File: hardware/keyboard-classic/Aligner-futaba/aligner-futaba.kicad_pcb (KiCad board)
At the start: 2 copper layers, 307.3 x 103.9 mm, 72 parts, among them SW1 Clear, SW10 Bracket_Open, SW11 6, SW12 Y, SW13 Return, SW14 Dash, SW15 5, SW16 T, SW17 Line Feed, SW18 Colon, SW19 4, SW2 Repeat, SW20 R, SW21 O, SW22 0, SW23 3, SW24 E, SW25 L, SW26 9, SW27 2, SW28 W, SW29 Period, SW3 Tilde, SW30 8, SW31 1, SW32 Ampersand, SW33 Break, SW34 Rubout, SW35 R_Shift, SW36 P, SW37 Comma, SW38 K, SW39 L_Shift, SW4 I, SW40 Semicolon, SW41 M, SW42 J, SW43 Fwd_Slash, SW44 N, SW45 H, SW46 SPACE, SW47 B, SW48 G, SW49 ESC, SW5 Here_is, SW50 Z, SW51 V, SW52 F, SW53 CTRL, SW54 A, SW55 C, SW56 D, SW57 Backslash, SW58 Q, SW59 X, SW6 Bracket_Close, SW60 S, SW7 7, SW8 U, SW9 Shift_Lock

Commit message: OSI mounting holes
- Add OSI-compatible mounting holes.
- Adjust keyboard and aligner holes to make room for the OSI mounting holes
- Change "Universal Keyboard" to "Unified Keyboard" in the design files.
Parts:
- removed the REF** at (107.8, 171.4)
- removed the REF** at (284.6, 171.4)
- removed the REF** at (363.2, 171.4)
- added REF**: MountingHole_3.5mm, MountingHole:MountingHole_3.5mm, F.Cu at (102.7, 171.4)
- added REF**: MountingHole_3.5mm, MountingHole:MountingHole_3.5mm, F.Cu at (289.7, 171.4)
- added REF**: MountingHole_3.5mm, MountingHole:MountingHole_3.5mm, F.Cu at (358.1, 171.4)
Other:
- board text added: "Unified Keyboard Rev 1.2 http://osiweb.org Key Aligner for Futaba MD-4PCS, George Risk KBM-01-01"
- board text removed: "Universal Keyboard Rev 1.1 http://osiweb.org Key Aligner for Futaba MD-4PCS, George Risk KBM-01-01"

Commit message: Finalize layout and mounting
- Add apple 2 mounting slots (and stretch PCB to accommodate slots
- Add pass-through holes in aligners for OSI keyboard spacers
- Move 'ESC' key next to '1' key
- Add TAB key next to Q key
- remove 'here is' and finalize "helper" keys along left side of keyboard
- move legends off of PCB traces
- update to release 1.3
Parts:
- removed the REF** at (72.1, 148.3)
- added REF**: FN, unikbd:Futaba-MD-4PCS-aligner, F.Cu at (82.8, 166.1)
- added REF**: OSI mounting holes, unikbd:OSI_spacer_holes, F.Cu at (196.9, 166.0)
- added REF**: OSHW-Logo2_9.8x8mm_SilkScreen, Symbol:OSHW-Logo2_9.8x8mm_SilkScreen, F.Cu at (146.6, 174.7)
- added SW62: ESC, unikbd:Futaba-MD-4PCS-aligner, F.Cu at (68.6, 89.8)
- SW1: value Clear -> RT arrow
- SW2: value Repeat -> LT arrow
- SW32: value Ampersand -> @ (at symbol)
- SW49: value ESC -> Tab
- SW5: value Here_is -> Repeat
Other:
- board size 307.3 x 103.9 mm -> 312.4 x 114 mm
- board text added: "Unified Keyboard Rev 1.3 http://osiweb.org Key Aligner for Futaba MD-4PCS, George Risk KBM-01-01"
- board text removed: "Unified Keyboard Rev 1.2 http://osiweb.org Key Aligner for Futaba MD-4PCS, George Risk KBM-01-01"

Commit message: Keyboard layout updates
- Add extra key to the left side of row 4 to permit "inverted T" for those who
  want it.

- Tiny shifts of several keys to correct key distances

- Include mounting holes with daughter board connector, to ensure consistency.
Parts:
- added REF**: Cherry aligner, unikbd:Cherry aligner, F.Cu at (263.8, 166.0)
- added REF**: Cherry aligner, unikbd:Cherry aligner, F.Cu at (130.5, 166.0)
- moved SW12 0.28 mm to (192.4, 108.8)
- moved SW17 0.28 mm to (287.6, 108.8)
- moved SW20 0.28 mm to (154.3, 108.8)
- moved SW22 0.28 mm to (249.5, 108.8)
- moved SW36 0.28 mm to (268.6, 108.8)
- moved SW8 0.28 mm to (211.4, 108.8)
- moved SW28 0.28 mm to (116.2, 108.8)
- moved SW58 0.28 mm to (97.1, 108.8)
- moved SW16 0.28 mm to (173.3, 108.8)
- moved SW24 0.28 mm to (135.2, 108.8)
- moved SW4 0.28 mm to (230.5, 108.8)
- moved SW13 0.24 mm to (311.5, 108.8)
- moved REF** 0.22 mm to (197.2, 166.0)
- moved SW46 0.22 mm to (197.2, 166.0)
- moved SW33 0.20 mm to (354.3, 108.8)
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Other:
- outline, holes or cut-outs redrawn
- board text added: "Unified Keyboard Rev 1.4 http://osiweb.org Key Aligner for Futaba MD-4PCS, George Risk KBM-01-01"
- board text removed: "Unified Keyboard Rev 1.3 http://osiweb.org Key Aligner for Futaba MD-4PCS, George Risk KBM-01-01"

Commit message: Moved mounting slots from keyboard PCB to aligners
- This allows the PCB to sink below the mounting brackets.  The aligner height can
be adjusted relative to the mounting brackets using spacers.

- changed futaba aligners to use cherry stabilizers.

- bumped rev number
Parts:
- removed the REF** at (263.8, 166.0)
- removed the REF** at (130.5, 166.0)
- SW46: footprint unikbd:Futaba-MD-4PCS-aligner -> unikbd:Futaba_space_Cherry_aligner
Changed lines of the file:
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@@
     (tracks 0)
     (zones 0)
-    (modules 77)
+    (modules 75)
     (nets 1)
   )
@@
     (visible_elements 7FFFEFFF)
     (pcbplotparams
-      (layerselection 0x010fc_ffffffff)
+      (layerselection 0x010f0_ffffffff)
       (usegerberextensions false)
       (usegerberattributes false)
@@
       (drillshape 0)
       (scaleselection 1)
-      (outputdirectory "futaba-aligner-outputs"))
+      (outputdirectory "outputs"))
   )
   (net 0 "")
@@
     (diff_pair_gap 0.254)
   )
-  (module "unikbd:Cherry aligner" (layer F.Cu)
-    (at 263.83488 165.99916)
-    (fp_text reference REF** (at -5.0292 -7.7724) (layer F.SilkS)
-      (effects (font (size 1 1) (thickness 0.15)))
-    )
-    (fp_text value "Cherry aligner" (at 0 7.9756) (layer B.Fab)
-      (effects (font (size 1 1) (thickness 0.15)))
-    )
-    (fp_line (start -6.985 -6.985) (end -6.985 6.985) (layer Edge.Cuts) (width 0.12))
-    (fp_line (start 6.985 6.985) (end 6.985 -6.985) (layer Edge.Cuts) (width 0.12))
-    (fp_line (start -6.985 -6.985) (end 6.985 -6.985) (layer Edge.Cuts) (width 0.12))
-    (fp_line (start -6.985 6.985) (end 6.985 6.985) (layer Edge.Cuts) (width 0.12))
-  )
-  (module "unikbd:Cherry aligner" (layer F.Cu)
-    (at 130.48488 165.99916)
-    (fp_text reference REF** (at -5.0292 -7.7724) (layer F.SilkS)
-      (effects (font (size 1 1) (thickness 0.15)))
-    )
-    (fp_text value "Cherry aligner" (at 0 7.9756) (layer B.Fab)
-      (effects (font (size 1 1) (thickness 0.15)))
-    )
-    (fp_line (start -6.985 -6.985) (end -6.985 6.985) (layer Edge.Cuts) (width 0.12))
-    (fp_line (start 6.985 6.985) (end 6.985 -6.985) (layer Edge.Cuts) (width 0.12))
-    (fp_line (start -6.985 -6.985) (end 6.985 -6.985) (layer Edge.Cuts) (width 0.12))
-    (fp_line (start -6.985 6.985) (end 6.985 6.985) (layer Edge.Cuts) (width 0.12))
+  (module unikbd:Futaba_space_Cherry_aligner (layer F.Cu)
+    (at 197.15988 165.99916)
+    (fp_text reference SW46 (at -4.62788 -8.77316) (layer F.SilkS)
+      (effects (font (size 1 1) (thickness 0.15)))
+    )
+    (fp_text value SPACE (at -3.35788 9.00684) (layer F.SilkS)
+      (effects (font (size 1 1) (thickness 0.15)))
+    )
+    (fp_text user MX_space_aligner (at -0.6096 7.9248) (layer B.Fab)
+      (effects (font (size 1 1) (thickness 0.15)))
+    )
+    (fp_text user SW** (at -5.334 -7.874) (layer F.SilkS)
+      (effects (font (size 1 1) (thickness 0.15)))
+    )
+    (fp_text user Futaba_2u_Cherry_aligner (at 0 -0.5) (layer F.Fab)
+      (effects (font (size 1 1) (thickness 0.15)))
+    )
+    (fp_text user REF** (at 0 0.5) (layer F.SilkS) hide
+      (effects (font (size 1 1) (thickness 0.15)))
+    )
+    (fp_line (start -63.3476 1.397) (end -7.6962 1.397) (layer Edge.Cuts) (width 0.12))
+    (fp_line (start -63.3476 -1.397) (end -7.6962 -1.397) (layer Edge.Cuts) (width 0.12))
+    (fp_line (start 7.6962 -1.397) (end 63.3476 -1.397) (layer Edge.Cuts) (width 0.12))
+    (fp_line (start 7.6962 1.397) (end 63.3476 1.397) (layer Edge.Cuts) (width 0.12))
+    (fp_arc (start 0 0) (end 7.697216 -1.397) (angle -159.4) (layer Edge.Cuts) (width 0.12))
+    (fp_arc (start 0 0) (end -7.697216 1.397) (angle -159.4) (layer Edge.Cuts) (width 0.12))
+    (fp_line (start 63.3476 -1.397) (end 63.3476 -5.6896) (layer Edge.Cuts) (width 0.12))
+    (fp_line (start 63.3476 -5.6896) (end 70.0024 -5.6896) (layer Edge.Cuts) (width 0.12))
+    (fp_line (start 70.0024 -5.6896) (end 70.0024 -2.286) (layer Edge.Cuts) (width 0.12))
+    (fp_line (start 70.0024 -2.286) (end 70.866 -2.286) (layer Edge.Cuts) (width 0.12))
+    (fp_line (start 70.866 -2.286) (end 70.866 0.508) (layer Edge.Cuts) (width 0.12))
+    (fp_line (start 70.866 0.508) (end 70.0024 0.508) (layer Edge.Cuts) (width 0.12))
+    (fp_line (start 70.0024 0.508) (end 70.0024 6.604) (layer Edge.Cuts) (width 0.12))
+    (fp_line (start 70.0024 6.604) (end 68.199 6.604) (layer Edge.Cuts) (width 0.12))
+    (fp_line (start 68.199 6.604) (end 68.199 7.7724) (layer Edge.Cuts) (width 0.12))
+    (fp_line (start 68.199 7.7724) (end 65.151 7.7724) (layer Edge.Cuts) (width 0.12))
+    (fp_line (start 65.151 7.7724) (end 65.151 6.604) (layer Edge.Cuts) (width 0.12))
+    (fp_line (start 65.151 6.604) (end 63.3476 6.604) (layer Edge.Cuts) (width 0.12))
+    (fp_line (start 63.3476 6.604) (end 63.3476 1.397) (layer Edge.Cuts) (width 0.12))
+    (fp_line (start -63.3476 1.397) (end -63.3476 6.604) (layer Edge.Cuts) (width 0.12))
+    (fp_line (start -63.3476 6.604) (end -65.151 6.604) (layer Edge.Cuts) (width 0.12))
+    (fp_line (start -65.151 6.604) (end -65.151 7.7724) (layer Edge.Cuts) (width 0.12))
+    (fp_line (start -65.151 7.7724) (end -68.199 7.7724) (layer Edge.Cuts) (width 0.12))
+    (fp_line (start -68.199 7.7724) (end -68.199 6.604) (layer Edge.Cuts) (width 0.12))
+    (fp_line (start -68.199 6.604) (end -70.0024 6.604) (layer Edge.Cuts) (width 0.12))
+    (fp_line (start -70.0024 6.604) (end -70.0024 0.508) (layer Edge.Cuts) (width 0.12))
+    (fp_line (start -70.0024 0.508) (end -70.866 0.508) (layer Edge.Cuts) (width 0.12))
+    (fp_line (start -70.866 0.508) (end -70.866 -2.286) (layer Edge.Cuts) (width 0.12))
+    (fp_line (start -70.866 -2.286) (end -70.0024 -2.286) (layer Edge.Cuts) (width 0.12))
+    (fp_line (start -70.0024 -2.286) (end -70.0024 -5.6896) (layer Edge.Cuts) (width 0.12))
+    (fp_line (start -70.0024 -5.6896) (end -63.3476 -5.6896) (layer Edge.Cuts) (width 0.12))
+    (fp_line (start -63.3476 -5.6896) (end -63.3476 -1.397) (layer Edge.Cuts) (width 0.12))
+    (pad "" np_thru_hole circle (at -6.985 6.985) (size 1.6256 1.6256) (drill 1.6256) (layers *.Cu *.Mask))
+    (pad "" np_thru_hole circle (at -6.985 -6.985) (size 1.6256 1.6256) (drill 1.6256) (layers *.Cu *.Mask))
+    (pad "" np_thru_hole circle (at 6.985 -6.985) (size 1.6256 1.6256) (drill 1.6256) (layers *.Cu *.Mask))
+    (pad "" np_thru_hole circle (at 6.985 6.985) (size 1.6256 1.6256) (drill 1.6256) (layers *.Cu *.Mask))
   )
   (module unikbd:Futaba-MD-4PCS-aligner locked (layer F.Cu)
@@
   (module unikbd:OSI_spacer_holes locked (layer F.Cu)
     (at 197.15988 165.99916)
-    (fp_text reference REF** (at 0 0.5) (layer F.SilkS)
+    (fp_text reference REF** (at 0 0.5) (layer F.SilkS) hide
       (effects (font (size 1 1) (thickness 0.15)))
     )
@@
     (pad 1 np_thru_hole circle (at 0 0) (size 3.5 3.5) (drill 3.5) (layers *.Cu *.Mask))
   )
-  (module unikbd:Futaba-MD-4PCS-aligner (layer F.Cu)
-    (at 197.15988 165.99916)
-    (fp_text reference SW46 (at -5.7912 -8.6106) (layer F.SilkS)
-      (effects (font (size 1 1) (thickness 0.15)))
-    )
-    (fp_text value SPACE (at -5.334 8.6614) (layer F.SilkS)
-      (effects (font (size 1 1) (thickness 0.15)))
-    )
-    (fp_circle (center 0 0) (end 7.8232 0) (layer Edge.Cuts) (width 0.12))
-    (pad "" np_thru_hole circle (at -6.985 -6.985) (size 1.6256 1.6256) (drill 1.6256) (layers *.Cu *.Mask))
-    (pad "" np_thru_hole circle (at -6.985 6.985) (size 1.6256 1.6256) (drill 1.6256) (layers *.Cu *.Mask))
-    (pad "" np_thru_hole circle (at 6.985 6.985) (size 1.6256 1.6256) (drill 1.6256) (layers *.Cu *.Mask))
-    (pad "" np_thru_hole circle (at 6.985 -6.985) (size 1.6256 1.6256) (drill 1.6256) (layers *.Cu *.Mask))
-  )
   (module unikbd:Futaba-MD-4PCS-aligner locked (layer F.Cu)

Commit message: Multiple fixes to classic keyboard for fit and build ease
- remove material from PCB to allow keyboard to fit in Apple II case

- enlarge center hole on cherry MX footprints slightly, to 0.160" to allow
slightly more tolerance, which eases assembly.

- include holes for LEDs on futaba aligner

- include extra pads on main PCB for LEDs with futaba keys

- Add LED on LINE FEED which maps to REPEAT/CAPSLOCK on Apple II keymap
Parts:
- removed the REF** at (82.9, 166.1)
- added SW61: FN, unikbd:Futaba-MD-4PCS-LED-aligner, F.Cu at (82.9, 166.0)
- SW1: value RT arrow -> RT Arrow
- SW17: footprint unikbd:Futaba-MD-4PCS-aligner -> unikbd:Futaba-MD-4PCS-LED-aligner
- SW2: value LT arrow -> LT Arrow
- SW32: value @ (at symbol) -> @ (AT)
- SW49: value Tab -> TAB
- SW9: value Shift_Lock -> Caps Lock; footprint unikbd:Futaba-MD-4PCS-aligner -> unikbd:Futaba-MD-4PCS-LED-aligner
- moved REF** 27.4 mm to (119.3, 174.2)
- moved SW33 0.20 mm to (354.1, 108.8)
- moved SW9 0.20 mm to (335.1, 108.8)
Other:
- outline, holes or cut-outs redrawn
- board text added: "Distances: Vertical: 0.75 inch Horizontal (1x - 1x): 0.75 inch Horizontal (1x - 1.5x): 0.975 inch Horizontal (Row 1 left key -> Row 2 left key): 0.375 inch Horizontal (Row 2 left key -> Row 3 left key): 0.1875 inch Horizontal (Row 3 left key -> Row 4 left key): 0.1875 inch Horizontal (Row 4 left key -> Row 5 left key): -0.1875 inch Horizontal (Row 5 left key -> space bar): 4.5 inch"
- board text added: "Unified Keyboard Rev 1.6 http://osiweb.org Cherry Key Aligner"
- board text removed: "Distances: Vertical: 0.75 inch Horizontal (1x - 1x): 0.75 inch Horizontal (1x - 1.5x): 0.939 inch Horizontal (Row 1 left key -> Row 2 left key): -0.379 inch Horizontal (Row 2 left key -> Row 3 left key): 0.187 inch Horizontal (Row 3 left key -> Row 4 left key): 0.186 inch Horizontal (Row 4 left key -> space bar): 4.310 inch"
- board text removed: "Unified Keyboard Rev 1.4 http://osiweb.org Key Aligner for Futaba MD-4PCS, George Risk KBM-01-01"

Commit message: Fixes for classic keyboard outline and mounting hole patters
- Adjust upper right corner circular cutout for AppleII+ case fit.

- Adjust OSI mounting hole pattern for improved fit.

- Changed OSI mount holes along top of keyboard to slots, to fit both C2P (542
keyboard) and C4P (542 Rev B/c keyboards).

- PCB and aligners must be slightly taller to accommodate the slots along the
top row
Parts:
- added REF**: MountingHole_2.1mm, MountingHole:MountingHole_2.1mm, F.Cu at (263.7, 177.4)
- added REF**: MountingHole_2.1mm, MountingHole:MountingHole_2.1mm, F.Cu at (130.3, 177.4)
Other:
- board size 312.4 x 114 mm -> 312.4 x 118.1 mm
- board text added: "File to 1.5mm"
- board text added: "Post Thickness Gauge"
- board text added: "Stabilizer bend guide"
- board text added: "Stabilzer bend guide"
- board text added: "Unified Keyboard Rev 1.7 http://osiweb.org Futaba Key Aligner"
- board text removed: "Unified Keyboard Rev 1.6 http://osiweb.org Cherry Key Aligner"

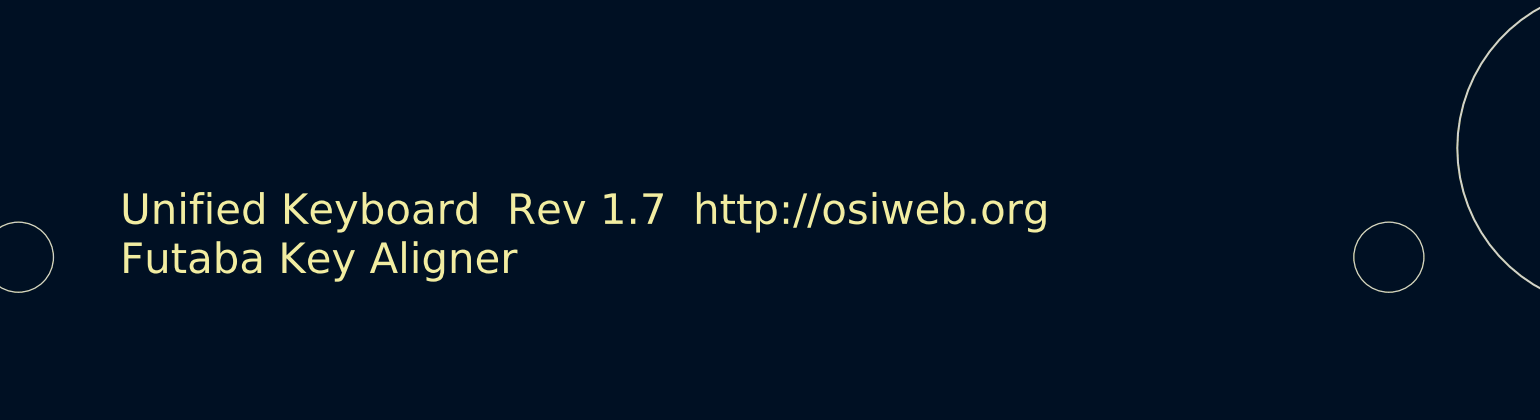
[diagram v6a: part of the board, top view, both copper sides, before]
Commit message: mechanical fit and buildability fixes
- Moved header slightly forward

- Moved interface mount holes do reduce interference with case mount holes

- For all keys in classic keyboard, add option for either through-hole or SMT
diodes and resistors.
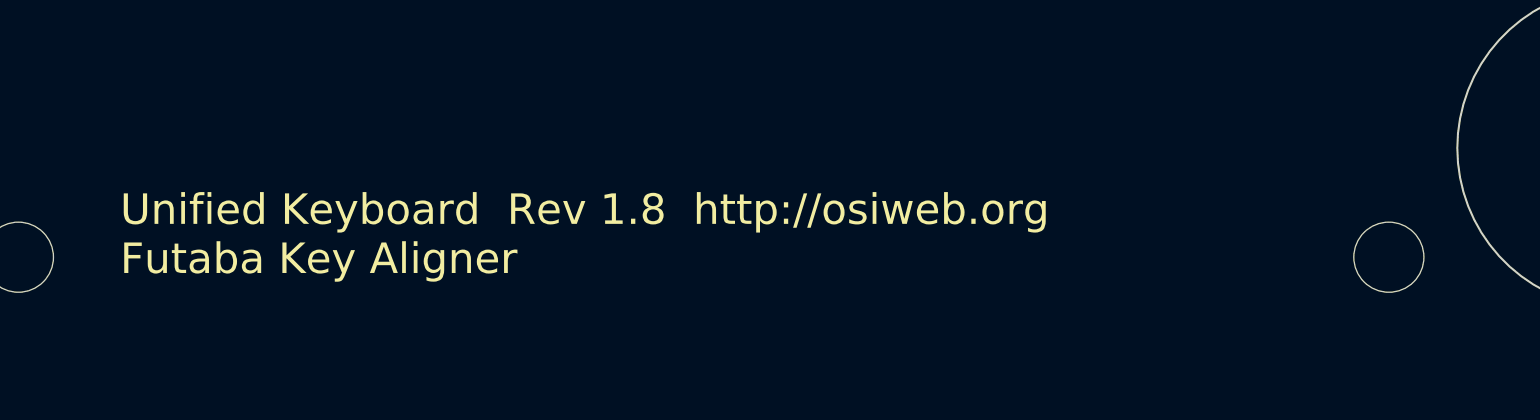
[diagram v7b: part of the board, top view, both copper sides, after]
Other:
- board text added: "Unified Keyboard Rev 1.8 http://osiweb.org Futaba Key Aligner"
- board text removed: "Unified Keyboard Rev 1.7 http://osiweb.org Futaba Key Aligner"

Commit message: Adjust some holes so interface mount holes double as aligner mounts.
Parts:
- removed the REF** at (289.7, 171.4)
- removed the REF** at (349.0, 78.7)
- removed the REF** at (300.7, 78.7)
- removed the REF** at (358.1, 171.4)
- added REF**: Interface mount, unikbd:kbd_mounting_holes_only, F.Cu at (301.0, 163.9)
